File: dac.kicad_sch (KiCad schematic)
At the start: 1 part, among them U16 DAC80504

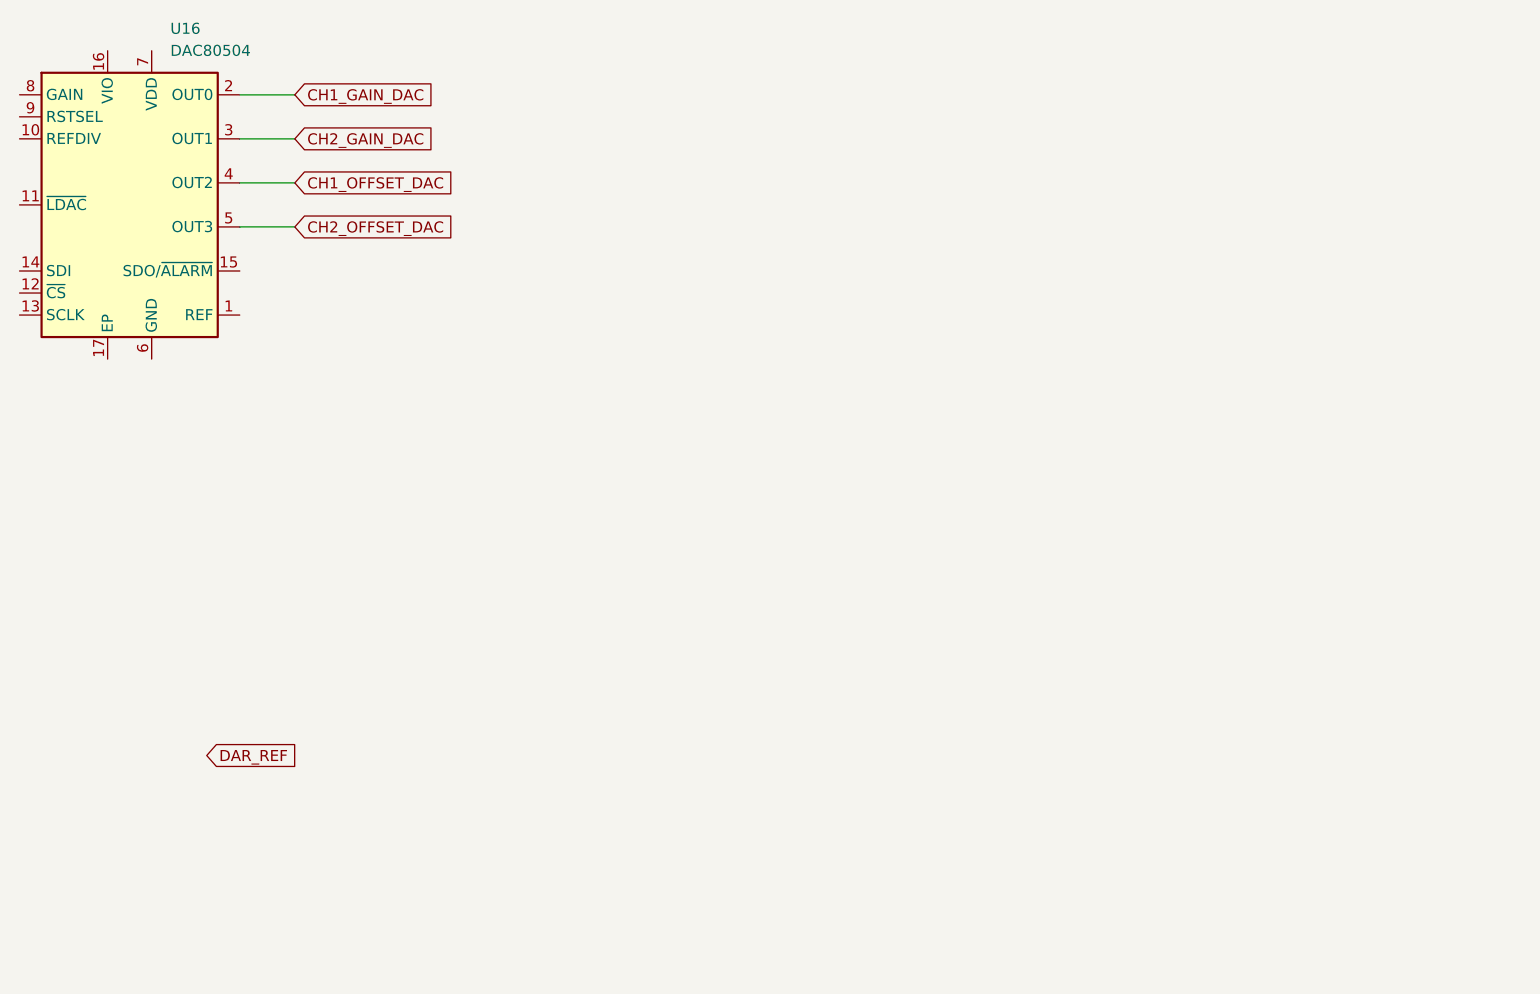
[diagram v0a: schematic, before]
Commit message: PCB edge, initial work on assigning footprints
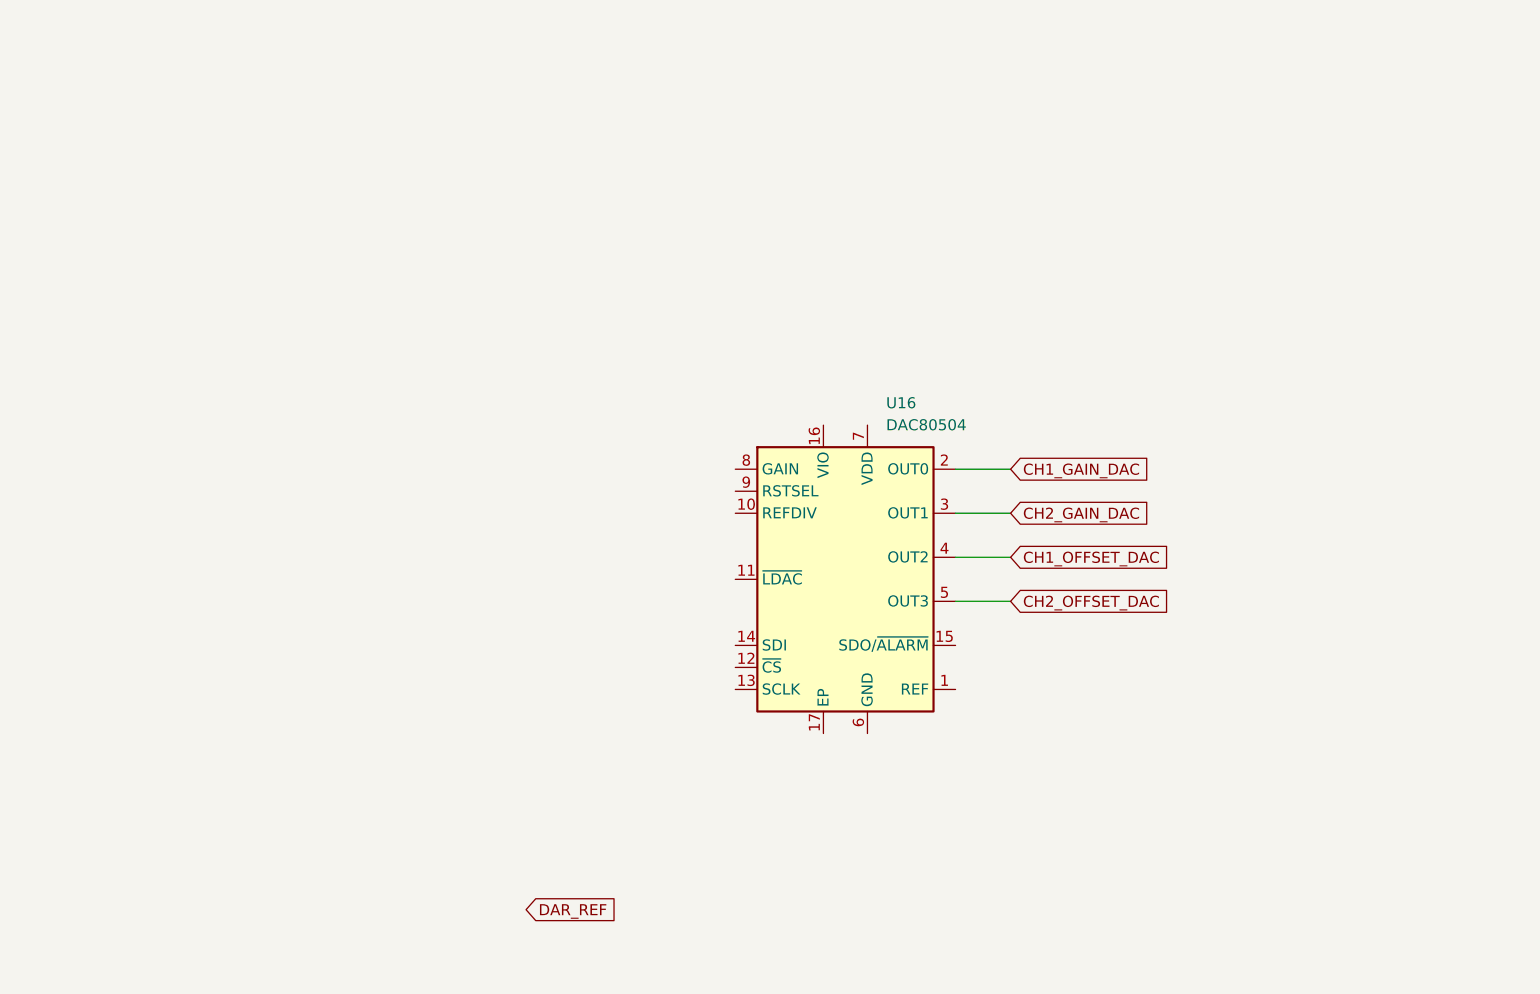
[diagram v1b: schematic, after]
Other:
- moved on the sheet: U16
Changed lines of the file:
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@@
 	(wire
 		(pts
-			(xy 50.8 31.75) (xy 44.45 31.75)
+			(xy 133.35 74.93) (xy 127 74.93)
 		)
 		(stroke
@@
 	(wire
 		(pts
-			(xy 50.8 36.83) (xy 44.45 36.83)
+			(xy 133.35 80.01) (xy 127 80.01)
 		)
 		(stroke
@@
 	(wire
 		(pts
-			(xy 50.8 41.91) (xy 44.45 41.91)
+			(xy 133.35 85.09) (xy 127 85.09)
 		)
 		(stroke
@@
 	(wire
 		(pts
-			(xy 50.8 26.67) (xy 44.45 26.67)
+			(xy 133.35 69.85) (xy 127 69.85)
 		)
 		(stroke
@@
 	(global_label "CH2_GAIN_DAC"
 		(shape input)
-		(at 50.8 31.75 0)
+		(at 133.35 74.93 0)
 		(fields_autoplaced yes)
 		(effects
@@
 		)
 		(property "Intersheetrefs" "${INTERSHEET_REFS}"
-			(at 67.4529 31.75 0)
+			(at 150.0029 74.93 0)
 			(effects
 				(font
@@
 	(global_label "CH2_OFFSET_DAC"
 		(shape input)
-		(at 50.8 41.91 0)
+		(at 133.35 85.09 0)
 		(fields_autoplaced yes)
 		(effects
@@
 		)
 		(property "Intersheetrefs" "${INTERSHEET_REFS}"
-			(at 69.9928 41.91 0)
+			(at 152.5428 85.09 0)
 			(effects
 				(font
@@
 	(global_label "CH1_OFFSET_DAC"
 		(shape input)
-		(at 50.8 36.83 0)
+		(at 133.35 80.01 0)
 		(fields_autoplaced yes)
 		(effects
@@
 		)
 		(property "Intersheetrefs" "${INTERSHEET_REFS}"
-			(at 69.9928 36.83 0)
+			(at 152.5428 80.01 0)
 			(effects
 				(font
@@
 	(global_label "CH1_GAIN_DAC"
 		(shape input)
-		(at 50.8 26.67 0)
+		(at 133.35 69.85 0)
 		(fields_autoplaced yes)
 		(effects
@@
 		)
 		(property "Intersheetrefs" "${INTERSHEET_REFS}"
-			(at 67.4529 26.67 0)
+			(at 150.0029 69.85 0)
 			(effects
 				(font
@@
 	(global_label "DAR_REF"
 		(shape input)
-		(at 40.64 102.87 0)
+		(at 77.47 120.65 0)
 		(fields_autoplaced yes)
 		(effects
@@
 		)
 		(property "Intersheetrefs" "${INTERSHEET_REFS}"
-			(at 51.729 102.87 0)
+			(at 88.559 120.65 0)
 			(effects
 				(font
@@
 	(symbol
 		(lib_id "Analog_DAC:DAC80504")
-		(at 31.75 39.37 0)
+		(at 114.3 82.55 0)
 		(unit 1)
 		(exclude_from_sim no)
@@
 		(fields_autoplaced yes)
 		(property "Reference" "U16"
-			(at 36.4333 19.05 0)
+			(at 118.9833 62.23 0)
 			(effects
 				(font
@@
 		)
 		(property "Value" "DAC80504"
-			(at 36.4333 21.59 0)
+			(at 118.9833 64.77 0)
 			(effects
 				(font
@@
 		)
 		(property "Footprint" "Package_DFN_QFN:Texas_RTE0016D_WQFN-16-1EP_3x3mm_P0.5mm_EP0.8x0.8mm_ThermalVias"
-			(at 31.75 39.37 0)
+			(at 114.3 82.55 0)
 			(effects
 				(font
@@
 		)
 		(property "Datasheet" "https://www.ti.com/lit/ds/symlink/dac80504.pdf"
-			(at 31.75 39.37 0)
+			(at 114.3 82.55 0)
 			(effects
 				(font
@@
 		)
 		(property "Description" "16-bit quad-channel voltage output DAC, 2.5V 2ppm/°C internal reference, WQFN-16"
-			(at 31.75 39.37 0)
+			(at 114.3 82.55 0)
 			(effects
 				(font

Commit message: Add things to MCU on the board
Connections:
- net SPI_1_CS: now reaches U16.12 (~{CS})
- net SPI_1_SCK: now reaches U16.13 (SCLK)
- net SPI_1_MOSI: now reaches U16.14 (SDI)
- net SPI_1_MISO: now reaches U16.15 (SDO/~{ALARM})
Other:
- moved on the sheet: U16
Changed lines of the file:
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@@
 	(wire
 		(pts
-			(xy 133.35 74.93) (xy 127 74.93)
-		)
-		(stroke
-			(width 0)
-			(type default)
-		)
-	)
-	(wire
-		(pts
-			(xy 133.35 80.01) (xy 127 80.01)
-		)
-		(stroke
-			(width 0)
-			(type default)
-		)
-	)
-	(wire
-		(pts
-			(xy 133.35 85.09) (xy 127 85.09)
-		)
-		(stroke
-			(width 0)
-			(type default)
-		)
-	)
-	(wire
-		(pts
-			(xy 133.35 69.85) (xy 127 69.85)
+			(xy 166.37 74.93) (xy 160.02 74.93)
+		)
+		(stroke
+			(width 0)
+			(type default)
+		)
+	)
+	(wire
+		(pts
+			(xy 130.81 92.71) (xy 134.62 92.71)
+		)
+		(stroke
+			(width 0)
+			(type default)
+		)
+	)
+	(wire
+		(pts
+			(xy 166.37 80.01) (xy 160.02 80.01)
+		)
+		(stroke
+			(width 0)
+			(type default)
+		)
+	)
+	(wire
+		(pts
+			(xy 166.37 90.17) (xy 160.02 90.17)
+		)
+		(stroke
+			(width 0)
+			(type default)
+		)
+	)
+	(wire
+		(pts
+			(xy 166.37 85.09) (xy 160.02 85.09)
+		)
+		(stroke
+			(width 0)
+			(type default)
+		)
+	)
+	(wire
+		(pts
+			(xy 130.81 90.17) (xy 134.62 90.17)
+		)
+		(stroke
+			(width 0)
+			(type default)
+		)
+	)
+	(wire
+		(pts
+			(xy 130.81 95.25) (xy 134.62 95.25)
+		)
+		(stroke
+			(width 0)
+			(type default)
+		)
+	)
+	(wire
+		(pts
+			(xy 166.37 69.85) (xy 160.02 69.85)
 		)
 		(stroke
@@
 	(global_label "CH2_GAIN_DAC"
 		(shape input)
-		(at 133.35 74.93 0)
-		(fields_autoplaced yes)
-		(effects
-			(font
-				(size 1.27 1.27)
-			)
-			(justify left)
-		)
-		(property "Intersheetrefs" "${INTERSHEET_REFS}"
-			(at 150.0029 74.93 0)
+		(at 166.37 74.93 0)
+		(fields_autoplaced yes)
+		(effects
+			(font
+				(size 1.27 1.27)
+			)
+			(justify left)
+		)
+		(property "Intersheetrefs" "${INTERSHEET_REFS}"
+			(at 183.0229 74.93 0)
 			(effects
 				(font
@@
 	(global_label "CH2_OFFSET_DAC"
 		(shape input)
-		(at 133.35 85.09 0)
-		(fields_autoplaced yes)
-		(effects
-			(font
-				(size 1.27 1.27)
-			)
-			(justify left)
-		)
-		(property "Intersheetrefs" "${INTERSHEET_REFS}"
-			(at 152.5428 85.09 0)
-			(effects
-				(font
-					(size 1.27 1.27)
-				)
-				(justify left)
+		(at 166.37 85.09 0)
+		(fields_autoplaced yes)
+		(effects
+			(font
+				(size 1.27 1.27)
+			)
+			(justify left)
+		)
+		(property "Intersheetrefs" "${INTERSHEET_REFS}"
+			(at 185.5628 85.09 0)
+			(effects
+				(font
+					(size 1.27 1.27)
+				)
+				(justify left)
+				(hide yes)
+			)
+		)
+	)
+	(global_label "SPI_1_MISO"
+		(shape input)
+		(at 166.37 90.17 0)
+		(fields_autoplaced yes)
+		(effects
+			(font
+				(size 1.27 1.27)
+			)
+			(justify left)
+		)
+		(property "Intersheetrefs" "${INTERSHEET_REFS}"
+			(at 180.1804 90.17 0)
+			(effects
+				(font
+					(size 1.27 1.27)
+				)
+				(justify left)
+				(hide yes)
+			)
+		)
+	)
+	(global_label "SPI_1_CS"
+		(shape input)
+		(at 130.81 92.71 180)
+		(fields_autoplaced yes)
+		(effects
+			(font
+				(size 1.27 1.27)
+			)
+			(justify right)
+		)
+		(property "Intersheetrefs" "${INTERSHEET_REFS}"
+			(at 119.1163 92.71 0)
+			(effects
+				(font
+					(size 1.27 1.27)
+				)
+				(justify right)
+				(hide yes)
+			)
+		)
+	)
+	(global_label "SPI_1_MOSI"
+		(shape input)
+		(at 130.81 90.17 180)
+		(fields_autoplaced yes)
+		(effects
+			(font
+				(size 1.27 1.27)
+			)
+			(justify right)
+		)
+		(property "Intersheetrefs" "${INTERSHEET_REFS}"
+			(at 116.9996 90.17 0)
+			(effects
+				(font
+					(size 1.27 1.27)
+				)
+				(justify right)
 				(hide yes)
 			)
@@
 	(global_label "CH1_OFFSET_DAC"
 		(shape input)
-		(at 133.35 80.01 0)
-		(fields_autoplaced yes)
-		(effects
-			(font
-				(size 1.27 1.27)
-			)
-			(justify left)
-		)
-		(property "Intersheetrefs" "${INTERSHEET_REFS}"
-			(at 152.5428 80.01 0)
-			(effects
-				(font
-					(size 1.27 1.27)
-				)
-				(justify left)
+		(at 166.37 80.01 0)
+		(fields_autoplaced yes)
+		(effects
+			(font
+				(size 1.27 1.27)
+			)
+			(justify left)
+		)
+		(property "Intersheetrefs" "${INTERSHEET_REFS}"
+			(at 185.5628 80.01 0)
+			(effects
+				(font
+					(size 1.27 1.27)
+				)
+				(justify left)
+				(hide yes)
+			)
+		)
+	)
+	(global_label "SPI_1_SCK"
+		(shape input)
+		(at 130.81 95.25 180)
+		(fields_autoplaced yes)
+		(effects
+			(font
+				(size 1.27 1.27)
+			)
+			(justify right)
+		)
+		(property "Intersheetrefs" "${INTERSHEET_REFS}"
+			(at 117.8463 95.25 0)
+			(effects
+				(font
+					(size 1.27 1.27)
+				)
+				(justify right)
 				(hide yes)
 			)
@@
 	(global_label "CH1_GAIN_DAC"
 		(shape input)
-		(at 133.35 69.85 0)
-		(fields_autoplaced yes)
-		(effects
-			(font
-				(size 1.27 1.27)
-			)
-			(justify left)
-		)
-		(property "Intersheetrefs" "${INTERSHEET_REFS}"
-			(at 150.0029 69.85 0)
+		(at 166.37 69.85 0)
+		(fields_autoplaced yes)
+		(effects
+			(font
+				(size 1.27 1.27)
+			)
+			(justify left)
+		)
+		(property "Intersheetrefs" "${INTERSHEET_REFS}"
+			(at 183.0229 69.85 0)
 			(effects
 				(font
@@
 	(global_label "DAR_REF"
 		(shape input)
-		(at 77.47 120.65 0)
-		(fields_autoplaced yes)
-		(effects
-			(font
-				(size 1.27 1.27)
-			)
-			(justify left)
-		)
-		(property "Intersheetrefs" "${INTERSHEET_REFS}"
-			(at 88.559 120.65 0)
+		(at 110.49 120.65 0)
+		(fields_autoplaced yes)
+		(effects
+			(font
+				(size 1.27 1.27)
+			)
+			(justify left)
+		)
+		(property "Intersheetrefs" "${INTERSHEET_REFS}"
+			(at 121.579 120.65 0)
 			(effects
 				(font
@@
 	(symbol
 		(lib_id "Analog_DAC:DAC80504")
-		(at 114.3 82.55 0)
+		(at 147.32 82.55 0)
 		(unit 1)
 		(exclude_from_sim no)
@@
 		(fields_autoplaced yes)
 		(property "Reference" "U16"
-			(at 118.9833 62.23 0)
+			(at 152.0033 62.23 0)
 			(effects
 				(font
@@
 		)
 		(property "Value" "DAC80504"
-			(at 118.9833 64.77 0)
+			(at 152.0033 64.77 0)
 			(effects
 				(font
@@
 		)
 		(property "Footprint" "Package_DFN_QFN:Texas_RTE0016D_WQFN-16-1EP_3x3mm_P0.5mm_EP0.8x0.8mm_ThermalVias"
-			(at 114.3 82.55 0)
+			(at 147.32 82.55 0)
 			(effects
 				(font
@@
 		)
 		(property "Datasheet" "https://www.ti.com/lit/ds/symlink/dac80504.pdf"
-			(at 114.3 82.55 0)
+			(at 147.32 82.55 0)
 			(effects
 				(font
@@
 		)
 		(property "Description" "16-bit quad-channel voltage output DAC, 2.5V 2ppm/°C internal reference, WQFN-16"
-			(at 114.3 82.55 0)
-			(effects
-				(font
+			(at 147.32 82.55 0)
+			(effects
+				(font

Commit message: Save work on simplifying the desing
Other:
- moved on the sheet: U16
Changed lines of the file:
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@@
 	(wire
 		(pts
-			(xy 166.37 74.93) (xy 160.02 74.93)
-		)
-		(stroke
-			(width 0)
-			(type default)
-		)
-	)
-	(wire
-		(pts
-			(xy 130.81 92.71) (xy 134.62 92.71)
-		)
-		(stroke
-			(width 0)
-			(type default)
-		)
-	)
-	(wire
-		(pts
-			(xy 166.37 80.01) (xy 160.02 80.01)
-		)
-		(stroke
-			(width 0)
-			(type default)
-		)
-	)
-	(wire
-		(pts
-			(xy 166.37 90.17) (xy 160.02 90.17)
-		)
-		(stroke
-			(width 0)
-			(type default)
-		)
-	)
-	(wire
-		(pts
-			(xy 166.37 85.09) (xy 160.02 85.09)
-		)
-		(stroke
-			(width 0)
-			(type default)
-		)
-	)
-	(wire
-		(pts
-			(xy 130.81 90.17) (xy 134.62 90.17)
-		)
-		(stroke
-			(width 0)
-			(type default)
-		)
-	)
-	(wire
-		(pts
-			(xy 130.81 95.25) (xy 134.62 95.25)
-		)
-		(stroke
-			(width 0)
-			(type default)
-		)
-	)
-	(wire
-		(pts
-			(xy 166.37 69.85) (xy 160.02 69.85)
+			(xy 158.75 71.12) (xy 152.4 71.12)
+		)
+		(stroke
+			(width 0)
+			(type default)
+		)
+	)
+	(wire
+		(pts
+			(xy 123.19 88.9) (xy 127 88.9)
+		)
+		(stroke
+			(width 0)
+			(type default)
+		)
+	)
+	(wire
+		(pts
+			(xy 158.75 76.2) (xy 152.4 76.2)
+		)
+		(stroke
+			(width 0)
+			(type default)
+		)
+	)
+	(wire
+		(pts
+			(xy 158.75 86.36) (xy 152.4 86.36)
+		)
+		(stroke
+			(width 0)
+			(type default)
+		)
+	)
+	(wire
+		(pts
+			(xy 158.75 81.28) (xy 152.4 81.28)
+		)
+		(stroke
+			(width 0)
+			(type default)
+		)
+	)
+	(wire
+		(pts
+			(xy 123.19 86.36) (xy 127 86.36)
+		)
+		(stroke
+			(width 0)
+			(type default)
+		)
+	)
+	(wire
+		(pts
+			(xy 123.19 91.44) (xy 127 91.44)
+		)
+		(stroke
+			(width 0)
+			(type default)
+		)
+	)
+	(wire
+		(pts
+			(xy 158.75 66.04) (xy 152.4 66.04)
 		)
 		(stroke
@@
 	(global_label "CH2_GAIN_DAC"
 		(shape input)
-		(at 166.37 74.93 0)
-		(fields_autoplaced yes)
-		(effects
-			(font
-				(size 1.27 1.27)
-			)
-			(justify left)
-		)
-		(property "Intersheetrefs" "${INTERSHEET_REFS}"
-			(at 183.0229 74.93 0)
+		(at 158.75 71.12 0)
+		(fields_autoplaced yes)
+		(effects
+			(font
+				(size 1.27 1.27)
+			)
+			(justify left)
+		)
+		(property "Intersheetrefs" "${INTERSHEET_REFS}"
+			(at 175.4029 71.12 0)
 			(effects
 				(font
@@
 	(global_label "CH2_OFFSET_DAC"
 		(shape input)
-		(at 166.37 85.09 0)
-		(fields_autoplaced yes)
-		(effects
-			(font
-				(size 1.27 1.27)
-			)
-			(justify left)
-		)
-		(property "Intersheetrefs" "${INTERSHEET_REFS}"
-			(at 185.5628 85.09 0)
+		(at 158.75 81.28 0)
+		(fields_autoplaced yes)
+		(effects
+			(font
+				(size 1.27 1.27)
+			)
+			(justify left)
+		)
+		(property "Intersheetrefs" "${INTERSHEET_REFS}"
+			(at 177.9428 81.28 0)
 			(effects
 				(font
@@
 	(global_label "SPI_1_MISO"
 		(shape input)
-		(at 166.37 90.17 0)
-		(fields_autoplaced yes)
-		(effects
-			(font
-				(size 1.27 1.27)
-			)
-			(justify left)
-		)
-		(property "Intersheetrefs" "${INTERSHEET_REFS}"
-			(at 180.1804 90.17 0)
+		(at 158.75 86.36 0)
+		(fields_autoplaced yes)
+		(effects
+			(font
+				(size 1.27 1.27)
+			)
+			(justify left)
+		)
+		(property "Intersheetrefs" "${INTERSHEET_REFS}"
+			(at 172.5604 86.36 0)
 			(effects
 				(font
@@
 	(global_label "SPI_1_CS"
 		(shape input)
-		(at 130.81 92.71 180)
+		(at 123.19 88.9 180)
 		(fields_autoplaced yes)
 		(effects
@@
 		)
 		(property "Intersheetrefs" "${INTERSHEET_REFS}"
-			(at 119.1163 92.71 0)
+			(at 111.4963 88.9 0)
 			(effects
 				(font
@@
 	(global_label "SPI_1_MOSI"
 		(shape input)
-		(at 130.81 90.17 180)
+		(at 123.19 86.36 180)
 		(fields_autoplaced yes)
 		(effects
@@
 		)
 		(property "Intersheetrefs" "${INTERSHEET_REFS}"
-			(at 116.9996 90.17 0)
+			(at 109.3796 86.36 0)
 			(effects
 				(font
@@
 	(global_label "CH1_OFFSET_DAC"
 		(shape input)
-		(at 166.37 80.01 0)
-		(fields_autoplaced yes)
-		(effects
-			(font
-				(size 1.27 1.27)
-			)
-			(justify left)
-		)
-		(property "Intersheetrefs" "${INTERSHEET_REFS}"
-			(at 185.5628 80.01 0)
+		(at 158.75 76.2 0)
+		(fields_autoplaced yes)
+		(effects
+			(font
+				(size 1.27 1.27)
+			)
+			(justify left)
+		)
+		(property "Intersheetrefs" "${INTERSHEET_REFS}"
+			(at 177.9428 76.2 0)
 			(effects
 				(font
@@
 	(global_label "SPI_1_SCK"
 		(shape input)
-		(at 130.81 95.25 180)
+		(at 123.19 91.44 180)
 		(fields_autoplaced yes)
 		(effects
@@
 		)
 		(property "Intersheetrefs" "${INTERSHEET_REFS}"
-			(at 117.8463 95.25 0)
+			(at 110.2263 91.44 0)
 			(effects
 				(font
@@
 	(global_label "CH1_GAIN_DAC"
 		(shape input)
-		(at 166.37 69.85 0)
-		(fields_autoplaced yes)
-		(effects
-			(font
-				(size 1.27 1.27)
-			)
-			(justify left)
-		)
-		(property "Intersheetrefs" "${INTERSHEET_REFS}"
-			(at 183.0229 69.85 0)
+		(at 158.75 66.04 0)
+		(fields_autoplaced yes)
+		(effects
+			(font
+				(size 1.27 1.27)
+			)
+			(justify left)
+		)
+		(property "Intersheetrefs" "${INTERSHEET_REFS}"
+			(at 175.4029 66.04 0)
 			(effects
 				(font
@@
 	(global_label "DAR_REF"
 		(shape input)
-		(at 110.49 120.65 0)
-		(fields_autoplaced yes)
-		(effects
-			(font
-				(size 1.27 1.27)
-			)
-			(justify left)
-		)
-		(property "Intersheetrefs" "${INTERSHEET_REFS}"
-			(at 121.579 120.65 0)
+		(at 166.37 101.6 0)
+		(fields_autoplaced yes)
+		(effects
+			(font
+				(size 1.27 1.27)
+			)
+			(justify left)
+		)
+		(property "Intersheetrefs" "${INTERSHEET_REFS}"
+			(at 177.459 101.6 0)
 			(effects
 				(font
@@
 	(symbol
 		(lib_id "Analog_DAC:DAC80504")
-		(at 147.32 82.55 0)
+		(at 139.7 78.74 0)
 		(unit 1)
 		(exclude_from_sim no)
@@
 		(fields_autoplaced yes)
 		(property "Reference" "U16"
-			(at 152.0033 62.23 0)
+			(at 144.3833 58.42 0)
 			(effects
 				(font
@@
 		)
 		(property "Value" "DAC80504"
-			(at 152.0033 64.77 0)
+			(at 144.3833 60.96 0)
 			(effects
 				(font
@@
 		)
 		(property "Footprint" "Package_DFN_QFN:Texas_RTE0016D_WQFN-16-1EP_3x3mm_P0.5mm_EP0.8x0.8mm_ThermalVias"
-			(at 147.32 82.55 0)
+			(at 139.7 78.74 0)
 			(effects
 				(font
@@
 		)
 		(property "Datasheet" "https://www.ti.com/lit/ds/symlink/dac80504.pdf"
-			(at 147.32 82.55 0)
+			(at 139.7 78.74 0)
 			(effects
 				(font
@@
 		)
 		(property "Description" "16-bit quad-channel voltage output DAC, 2.5V 2ppm/°C internal reference, WQFN-16"
-			(at 147.32 82.55 0)
-			(effects
-				(font
+			(at 139.7 78.74 0)
+			(effects
+				(font
